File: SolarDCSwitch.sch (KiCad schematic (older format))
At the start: 3 parts

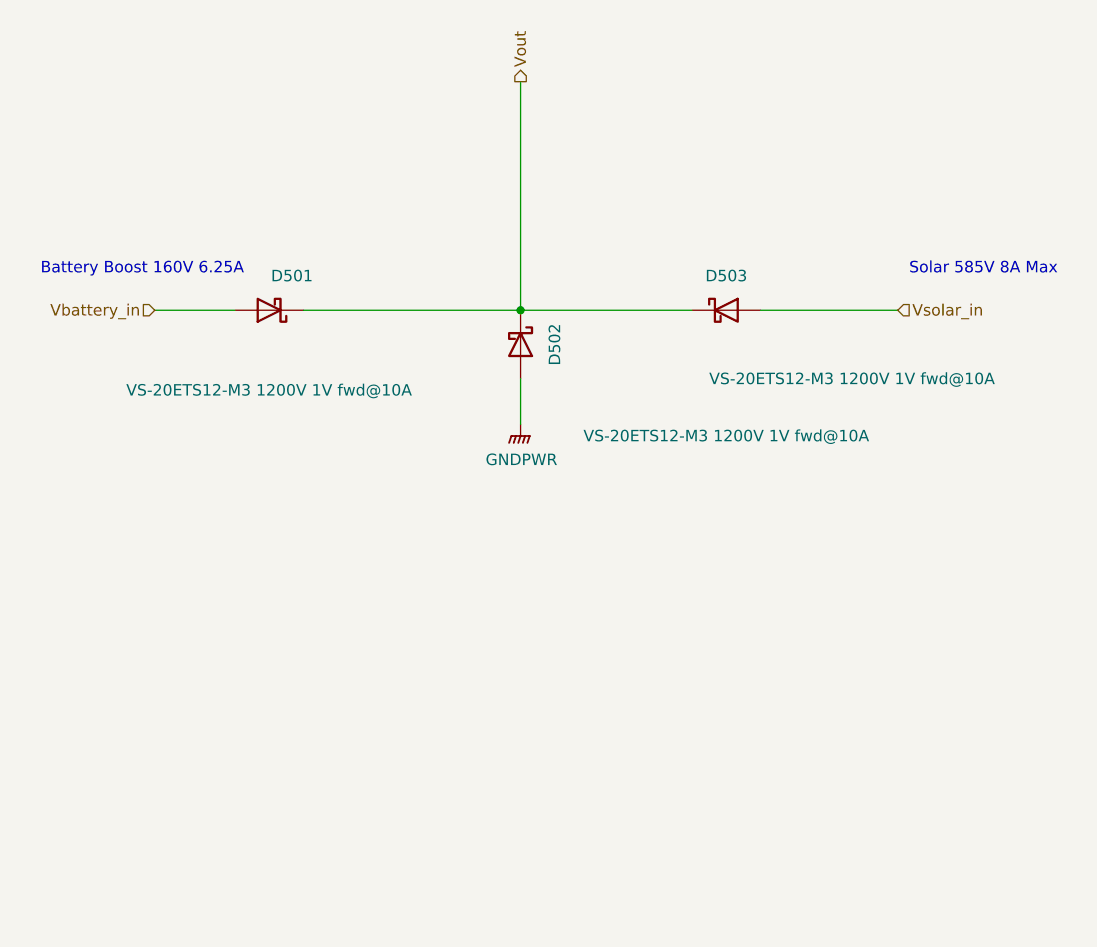
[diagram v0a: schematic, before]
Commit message: Added voltage divider network and input protection to measure, the Solar input voltage, I decided this would be usefull in the cases where the solar is producing voltage over 160V, but the house is stillimporting power from the Grid, there is not point in powering up the boost converter because we can't get power into the system, as output is 160V.  Also update the TestPoint footprints to match the latest Kicad naming convention, simular to my resistor and capacitor footprint changes a few commits ago.
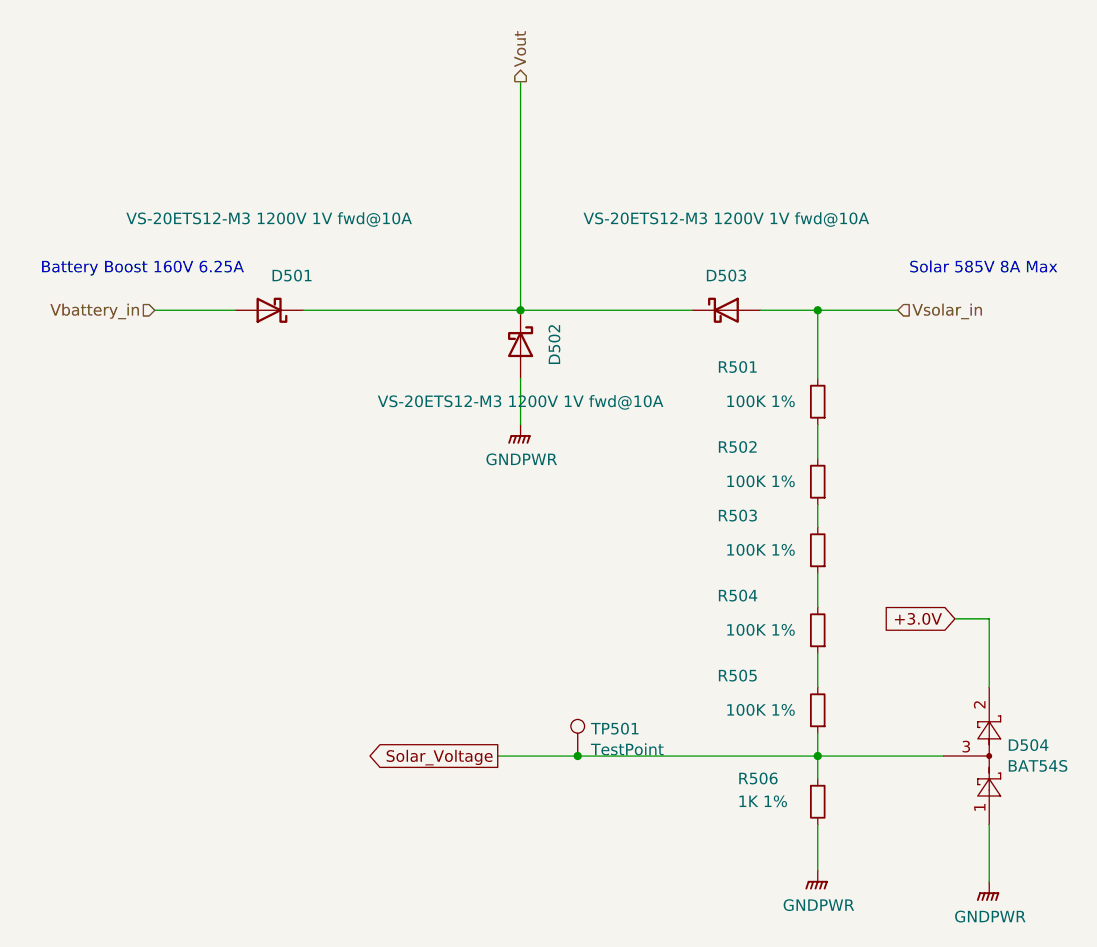
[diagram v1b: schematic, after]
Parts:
- added D504: BAT54S, Package_TO_SOT_SMD:SOT-23_Handsoldering, symbol Diode:BAT54S
- added R501, R502, R503, R504, R505: 100K 1%, Resistor_SMD:R_0805_2012Metric_Pad1.15x1.40mm_HandSolder, symbol Device:R_Small
- added R506: 1K 1%, Resistor_SMD:R_0805_2012Metric_Pad1.15x1.40mm_HandSolder, symbol Device:R_Small
- added TP501: TestPoint, TestPoint:TestPoint_Pad_3.0x3.0mm, symbol Connector:TestPoint
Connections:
- net GNDPWR: now also D504.1, R506.2
- net Vsolar_in: now also R501.2
- new net: R501.1, R502.2
- new net: R502.1, R503.2
- new net: R503.1, R504.2
- new net: R504.1, R505.2
- new net +3.0V: D504.2
- new net Solar_Voltage: D504.3, R505.1, R506.1, TP501.1
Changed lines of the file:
@@
 AR Path="/5F4EB1AC/5EBD6C25" Ref="D501"  Part="1"
 F 0 "D501" H 3150 3750 50  0000 C CNN
-F 1 "VS-20ETS12-M3 1200V 1V fwd@10A" H 3250 4250 50  0000 C CNN
+F 1 "VS-20ETS12-M3 1200V 1V fwd@10A" H 3250 3500 50  0000 C CNN
 F 2 "Diodes_ThroughHole_jl:Diode_TO_220AC_Horizonal" H 3250 3900 50  0001 C CNN
 F 3 "http://www.vishay.com/docs/96244/vs-20etsm3_vs-20atsm3.pdf" H 3250 3900 50  0001 C CNN
@@
 AR Path="/5F4EB1AC/5EBD7949" Ref="D503"  Part="1"
 F 0 "D503" H 5250 4050 50  0000 C CNN
-F 1 "VS-20ETS12-M3 1200V 1V fwd@10A" H 5800 3600 50  0000 C CNN
+F 1 "VS-20ETS12-M3 1200V 1V fwd@10A" H 5250 4300 50  0000 C CNN
 F 2 "Diodes_ThroughHole_jl:Diode_TO_220AC_Horizonal" H 5250 3900 50  0001 C CNN
 F 3 "http://www.vishay.com/docs/96244/vs-20etsm3_vs-20atsm3.pdf" H 5250 3900 50  0001 C CNN
@@
 AR Path="/5F4EB1AC/5EC134A6" Ref="D502"  Part="1"
 F 0 "D502" H 4350 4200 50  0000 C CNN
-F 1 "VS-20ETS12-M3 1200V 1V fwd@10A" V 4750 4950 50  0000 C CNN
+F 1 "VS-20ETS12-M3 1200V 1V fwd@10A" V 4600 4050 50  0000 C CNN
 F 2 "Diodes_ThroughHole_jl:Diode_TO_220AC_Horizonal" H 4350 4050 50  0001 C CNN
 F 3 "http://www.vishay.com/docs/96244/vs-20etsm3_vs-20atsm3.pdf" H 4350 4050 50  0001 C CNN
@@
 	4350 3900 4350 2900
 Wire Wire Line
-	5400 3900 6000 3900
-Wire Wire Line
 	4350 4400 4350 4200
 Connection ~ 4350 3900
+$Comp
+L Device:R_Small R?
+U 1 1 5F3D7AA3
+P 5650 4300
+AR Path="/5EF73D52/5F3D7AA3" Ref="R?"  Part="1"
+AR Path="/5F4EB1AC/5F3D7AA3" Ref="R501"  Part="1"
+F 0 "R501" H 6000 4150 50  0000 C CNN
+F 1 "100K 1%" H 5900 4300 50  0000 C CNN
+F 2 "Resistor_SMD:R_0805_2012Metric_Pad1.15x1.40mm_HandSolder" H 5650 4300 50  0001 C CNN
+F 3 "https://www.yageo.com/upload/media/product/productsearch/datasheet/rchip/PYu-RC_Group_51_RoHS_L_11.pdf" H 5650 4300 50  0001 C CNN
+F 4 "Yageo" H 4000 1700 50  0001 C CNN "MFR"
+F 5 "RC0805FR-07100KL" H 4000 1700 50  0001 C CNN "MPN"
+F 6 "digikey" H 4000 1700 50  0001 C CNN "SPR"
+F 7 "311-100KCRCT-ND" H 4000 1700 50  0001 C CNN "SPN"
+F 8 "-" H 4000 1700 50  0001 C CNN "SPURL"
+	1    5650 4300
+	-1   0    0    1
+$EndComp
+$Comp
+L Device:R_Small R?
+U 1 1 5F3D7B25
+P 5650 4650
+AR Path="/5EF73D52/5F3D7B25" Ref="R?"  Part="1"
+AR Path="/5F4EB1AC/5F3D7B25" Ref="R502"  Part="1"
+F 0 "R502" H 6000 4500 50  0000 C CNN
+F 1 "100K 1%" H 5900 4650 50  0000 C CNN
+F 2 "Resistor_SMD:R_0805_2012Metric_Pad1.15x1.40mm_HandSolder" H 5650 4650 50  0001 C CNN
+F 3 "https://www.yageo.com/upload/media/product/productsearch/datasheet/rchip/PYu-RC_Group_51_RoHS_L_11.pdf" H 5650 4650 50  0001 C CNN
+F 4 "Yageo" H 4000 2050 50  0001 C CNN "MFR"
+F 5 "RC0805FR-07100KL" H 4000 2050 50  0001 C CNN "MPN"
+F 6 "digikey" H 4000 2050 50  0001 C CNN "SPR"
+F 7 "311-100KCRCT-ND" H 4000 2050 50  0001 C CNN "SPN"
+F 8 "-" H 4000 2050 50  0001 C CNN "SPURL"
+	1    5650 4650
+	-1   0    0    1
+$EndComp
+$Comp
+L Device:R_Small R?
+U 1 1 5F3D8114
+P 5650 4950
+AR Path="/5EF73D52/5F3D8114" Ref="R?"  Part="1"
+AR Path="/5F4EB1AC/5F3D8114" Ref="R503"  Part="1"
+F 0 "R503" H 6000 4800 50  0000 C CNN
+F 1 "100K 1%" H 5900 4950 50  0000 C CNN
+F 2 "Resistor_SMD:R_0805_2012Metric_Pad1.15x1.40mm_HandSolder" H 5650 4950 50  0001 C CNN
+F 3 "https://www.yageo.com/upload/media/product/productsearch/datasheet/rchip/PYu-RC_Group_51_RoHS_L_11.pdf" H 5650 4950 50  0001 C CNN
+F 4 "Yageo" H 4000 2350 50  0001 C CNN "MFR"
+F 5 "RC0805FR-07100KL" H 4000 2350 50  0001 C CNN "MPN"
+F 6 "digikey" H 4000 2350 50  0001 C CNN "SPR"
+F 7 "311-100KCRCT-ND" H 4000 2350 50  0001 C CNN "SPN"
+F 8 "-" H 4000 2350 50  0001 C CNN "SPURL"
+	1    5650 4950
+	-1   0    0    1
+$EndComp
+$Comp
+L Device:R_Small R?
+U 1 1 5F3D860D
+P 5650 5300
+AR Path="/5EF73D52/5F3D860D" Ref="R?"  Part="1"
+AR Path="/5F4EB1AC/5F3D860D" Ref="R504"  Part="1"
+F 0 "R504" H 6000 5150 50  0000 C CNN
+F 1 "100K 1%" H 5900 5300 50  0000 C CNN
+F 2 "Resistor_SMD:R_0805_2012Metric_Pad1.15x1.40mm_HandSolder" H 5650 5300 50  0001 C CNN
+F 3 "https://www.yageo.com/upload/media/product/productsearch/datasheet/rchip/PYu-RC_Group_51_RoHS_L_11.pdf" H 5650 5300 50  0001 C CNN
+F 4 "Yageo" H 4000 2700 50  0001 C CNN "MFR"
+F 5 "RC0805FR-07100KL" H 4000 2700 50  0001 C CNN "MPN"
+F 6 "digikey" H 4000 2700 50  0001 C CNN "SPR"
+F 7 "311-100KCRCT-ND" H 4000 2700 50  0001 C CNN "SPN"
+F 8 "-" H 4000 2700 50  0001 C CNN "SPURL"
+	1    5650 5300
+	-1   0    0    1
+$EndComp
+$Comp
+L Device:R_Small R?
+U 1 1 5F3D8A24
+P 5650 5650
+AR Path="/5EF73D52/5F3D8A24" Ref="R?"  Part="1"
+AR Path="/5F4EB1AC/5F3D8A24" Ref="R505"  Part="1"
+F 0 "R505" H 6000 5500 50  0000 C CNN
+F 1 "100K 1%" H 5900 5650 50  0000 C CNN
+F 2 "Resistor_SMD:R_0805_2012Metric_Pad1.15x1.40mm_HandSolder" H 5650 5650 50  0001 C CNN
+F 3 "https://www.yageo.com/upload/media/product/productsearch/datasheet/rchip/PYu-RC_Group_51_RoHS_L_11.pdf" H 5650 5650 50  0001 C CNN
+F 4 "Yageo" H 4000 3050 50  0001 C CNN "MFR"
+F 5 "RC0805FR-07100KL" H 4000 3050 50  0001 C CNN "MPN"
+F 6 "digikey" H 4000 3050 50  0001 C CNN "SPR"
+F 7 "311-100KCRCT-ND" H 4000 3050 50  0001 C CNN "SPN"
+F 8 "-" H 4000 3050 50  0001 C CNN "SPURL"
+	1    5650 5650
+	-1   0    0    1
+$EndComp
+$Comp
+L Device:R_Small R?
+U 1 1 5F3E961C
+P 5650 6050
+AR Path="/5F3E961C" Ref="R?"  Part="1"
+AR Path="/5F4EB1AC/5F3E961C" Ref="R506"  Part="1"
+F 0 "R506" H 5300 6150 50  0000 L CNN
+F 1 "1K 1%" H 5300 6050 50  0000 L CNN
+F 2 "Resistor_SMD:R_0805_2012Metric_Pad1.15x1.40mm_HandSolder" H 5650 6050 50  0001 C CNN
+F 3 "https://www.yageo.com/upload/media/product/productsearch/datasheet/rchip/PYu-RC_Group_51_RoHS_L_11.pdf" H 5650 6050 50  0001 C CNN
+F 4 "Yageo" H 3050 1800 50  0001 C CNN "MFR"
+F 5 "RC0805FR-071KL" H 3050 1800 50  0001 C CNN "MPN"
+F 6 "digikey" H 3050 1800 50  0001 C CNN "SPR"
+F 7 "311-1.00KCRCT-ND" H 3050 1800 50  0001 C CNN "SPN"
+F 8 "-" H 3050 1800 50  0001 C CNN "SPURL"
+	1    5650 6050
+	1    0    0    -1
+$EndComp
+Wire Wire Line
+	5650 4400 5650 4550
+Wire Wire Line
+	5650 4750 5650 4850
+Wire Wire Line
+	5650 5050 5650 5200
+Wire Wire Line
+	5650 5400 5650 5550
+Wire Wire Line
+	5650 5750 5650 5850
+$Comp
+L power:GNDPWR #PWR0502
+U 1 1 5F3ECBA7
+P 5650 6350
+F 0 "#PWR0502" H 5650 6150 50  0001 C CNN
+F 1 "GNDPWR" H 5654 6196 50  0000 C CNN
+F 2 "" H 5650 6300 50  0001 C CNN
+F 3 "" H 5650 6300 50  0001 C CNN
+	1    5650 6350
+	1    0    0    -1
+$EndComp
+Wire Wire Line
+	5650 6150 5650 6350
+Wire Wire Line
+	5400 3900 5650 3900
+Connection ~ 5650 3900
+Wire Wire Line
+	5650 3900 6000 3900
+$Comp
+L Diode:BAT54S D?
+U 1 1 5F407A9C
+P 6400 5850
+AR Path="/5F15BF3C/5F407A9C" Ref="D?"  Part="1"
+AR Path="/5F407A9C" Ref="D?"  Part="1"
+AR Path="/5F4EB1AC/5F407A9C" Ref="D504"  Part="1"
+F 0 "D504" V 6446 5929 50  0000 L CNN
+F 1 "BAT54S" V 6355 5929 50  0000 L CNN
+F 2 "Package_TO_SOT_SMD:SOT-23_Handsoldering" H 6400 5350 50  0001 C CNN
+F 3 "http://toshiba.semicon-storage.com/info/docget.jsp?did=37137&prodName=TBAT54" H 6400 5850 50  0001 C CNN
+F 4 "Toshiba Semiconductor and Storage" H 2100 -1000 50  0001 C CNN "MFR"
+F 5 "TBAT54S,LM" H 2100 -1000 50  0001 C CNN "MPN"
+F 6 "digikey" H 2100 -1000 50  0001 C CNN "SPR"
+F 7 "TBAT54SLMCT-ND" H 2100 -1000 50  0001 C CNN "SPN"
+F 8 "-" H 2100 -1000 50  0001 C CNN "SPURL"
+	1    6400 5850
+	0    1    -1   0
+$EndComp
+$Comp
+L power:GNDPWR #PWR?
+U 1 1 5F407AA2
+P 6400 6400
+AR Path="/5F407AA2" Ref="#PWR?"  Part="1"
+AR Path="/5F4EB1AC/5F407AA2" Ref="#PWR0503"  Part="1"
+F 0 "#PWR0503" H 6400 6200 50  0001 C CNN
+F 1 "GNDPWR" H 6404 6246 50  0000 C CNN
+F 2 "" H 6400 6350 50  0001 C CNN
+F 3 "" H 6400 6350 50  0001 C CNN
+	1    6400 6400
+	1    0    0    -1
+$EndComp
+Text GLabel 6250 5250 0    50   Input ~ 0
++3.0V
+Wire Wire Line
+	6250 5250 6400 5250
+Wire Wire Line
+	6400 5250 6400 5550
+Wire Wire Line
+	6400 6150 6400 6400
+Wire Wire Line
+	5650 5850 6200 5850
+Connection ~ 5650 5850
+Wire Wire Line
+	5650 5850 5650 5950
+Text GLabel 4250 5850 0    50   Output ~ 0
+Solar_Voltage
+Wire Wire Line
+	5650 5850 4600 5850
+$Comp
+L Connector:TestPoint TP?
+U 1 1 5F487196
+P 4600 5850
+AR Path="/5EBD6442/5F487196" Ref="TP?"  Part="1"
+AR Path="/5EF73D52/5F487196" Ref="TP?"  Part="1"
+AR Path="/5F487196" Ref="TP?"  Part="1"
+AR Path="/5F4EB1AC/5F487196" Ref="TP501"  Part="1"
+F 0 "TP501" H 4658 5968 50  0000 L CNN
+F 1 "TestPoint" H 4658 5877 50  0000 L CNN
+F 2 "TestPoint:TestPoint_Pad_3.0x3.0mm" H 4800 5850 50  0001 C CNN
+F 3 "~" H 4800 5850 50  0001 C CNN
+F 4 "-" H 3150 -450 50  0001 C CNN "MFR"
+F 5 "-" H 3150 -450 50  0001 C CNN "MPN"
+F 6 "-" H 3150 -450 50  0001 C CNN "SPR"
+F 7 "-" H 3150 -450 50  0001 C CNN "SPN"
+F 8 "-" H 3150 -450 50  0001 C CNN "SPURL"
+	1    4600 5850
+	1    0    0    -1
+$EndComp
+Connection ~ 4600 5850
+Wire Wire Line
+	4600 5850 4250 5850
+Wire Wire Line
+	5650 3900 5650 4200
 $EndSCHEMATC
